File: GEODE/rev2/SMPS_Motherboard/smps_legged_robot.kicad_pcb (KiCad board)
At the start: 6 copper layers, 204.5 x 71.7 mm, 312 parts, among them IC1101 LAN9252_ML, IC1102 M24C16-RMN6P, IC1201 MAX25262AFOF_VY+, IC1501 TPS2490DGSRG4, IC1701 TPA6205A1DGN, IC2001 INA239AQDGSRQ1, IC801 TPS629206QDRLRQ1, J1 FTSH-105-01-F-D-RA-K, J1102 Nano-Fit 1x03, J1104 Nano-Fit 1x03, J1107 RJ45_Wuerth_74980111211, J1108 RJ45_Wuerth_74980111211, J1110 PTH 01x03 2.54mm, J1301 10159558-410421RLF, J1701 53048-0450, J1702 505110-3091, J1801 S2B-PH-SM4-TB, J2 XT30PW-M, J2501 10159558-410421RLF, J3 XT30PW-M, J301 Rail 1, J302 Rail 2, J303 Rail 3, J304 Rail 4, J305 Vin, J306 VBAT, J4 XT30PW-M, J403 USB4105-GF-A, J501 XT90PW-M, J502 XT90PW-F, J7 502585-0470, J8 XT30PW-M, Q1101 SOT233 ZXMP10A13F, Q1102 SOT233 BSS123N, Q1201 SQJQ186E-T1_GE3, Q1202 SQJQ186E-T1_GE3, Q1203 SQJQ186E-T1_GE3, Q1204 SQJQ186E-T1_GE3, Q1401 PMV90ENER, Q801 PMV90ENER, Q802 PMV90ENER, SW1101 CAS-220TA, U1102 TCAN1051HGVDRBRQ1, U1501 MCP9700BT-E/TT, U1701 74LVC1G125, U1801 DGD0216WT-7, U401 STM32G483RET6, U801 TPS2116DRLR, U802 LMR36506MSC5RPERQ1, Y1101 7M-25.000MAAJ-T, Y401 ABM8W-48.0000MHZ-4-D1X-T3

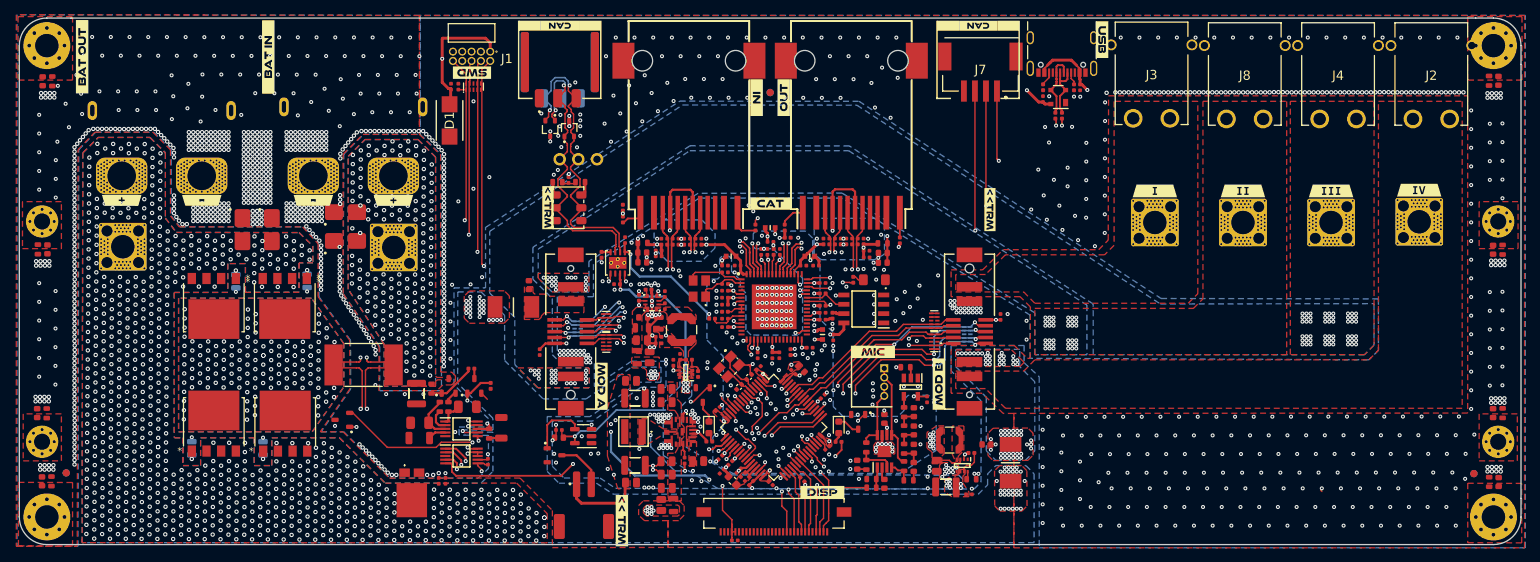
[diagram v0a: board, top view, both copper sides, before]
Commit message: added xt30 connectors to layout moved screw holes
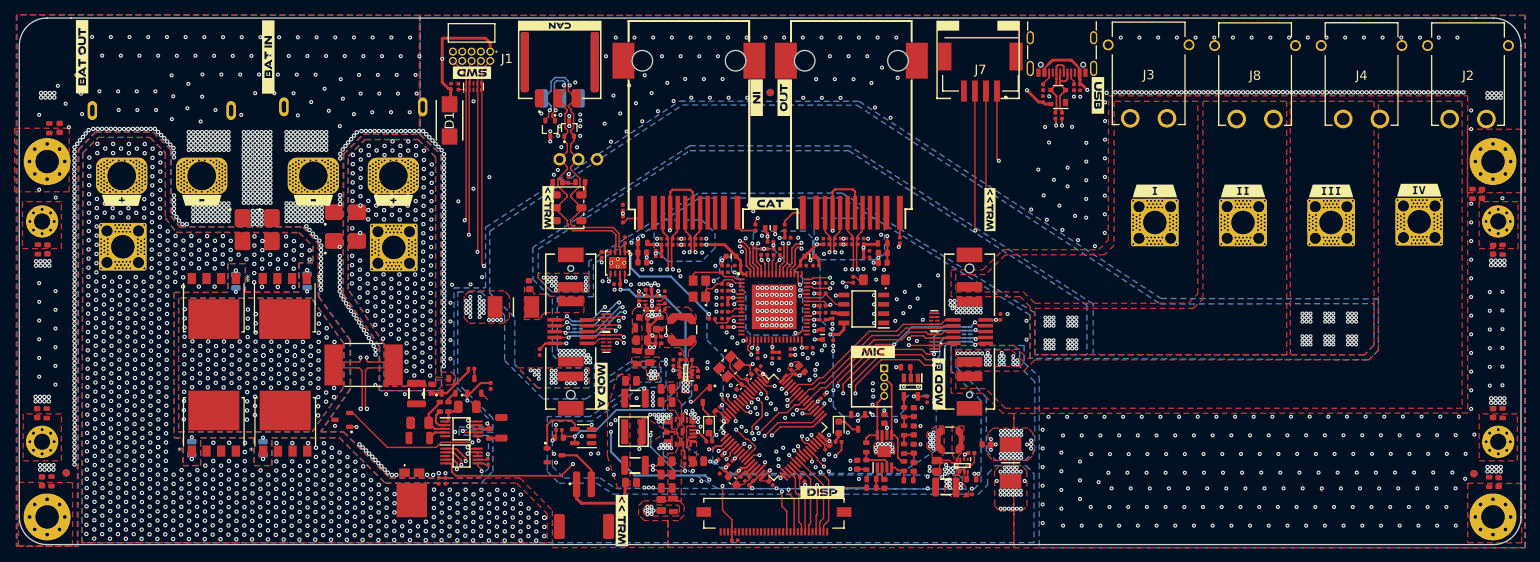
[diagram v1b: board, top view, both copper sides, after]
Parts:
- removed kibuzzard-657DB620: G***, kibuzzard-657DB620
- moved H2204 15.8 mm to (248.7, 72.2)
- moved H2201 15.8 mm to (51.8, 72.2)
- moved R2204 15.6 mm to (245.9, 76.6)
- moved C2204 15.6 mm to (247.2, 76.6)
- moved kibuzzard-664858D5 7.62 mm to (194.9, 63.2)
- moved C2201 6.74 mm to (53.5, 67.6), turned to 90 degrees
- moved R2201 6.41 mm to (52.1, 67.7), turned to 90 degrees
- moved J2 5.00 mm to (245.3, 60.5)
- moved J4 3.20 mm to (230.8, 60.5)
- moved J8 1.40 mm to (216.3, 60.5)
- moved J3 0.40 mm to (201.8, 60.4)
- moved H2203 0.06 mm to (248.7, 120.6)
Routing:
- net GND: vias 1468 -> 1451
